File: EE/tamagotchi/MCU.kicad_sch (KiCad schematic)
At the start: 5 parts, among them J7 TAG_CONNECT, U2 STM32G031G8Ux

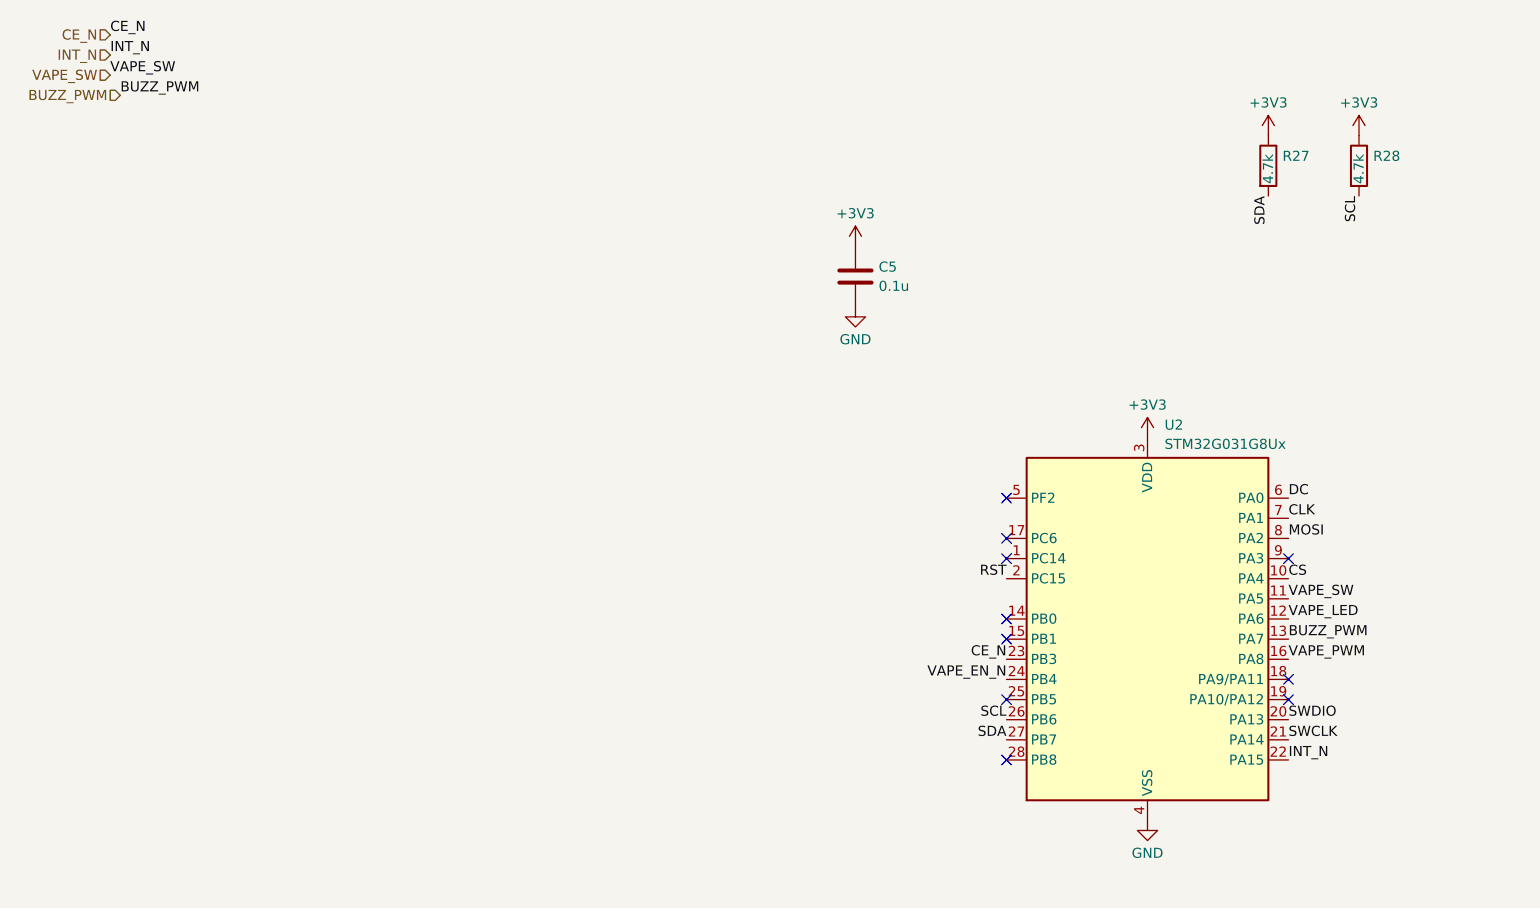
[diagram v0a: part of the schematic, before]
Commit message: WIP - Overall Cleanup, Power Change
Added expected loads for power in schematic.
Changed power arch to use existing design that appears to work.
Removed rear backlight LEDs - shouldn't be necessary.
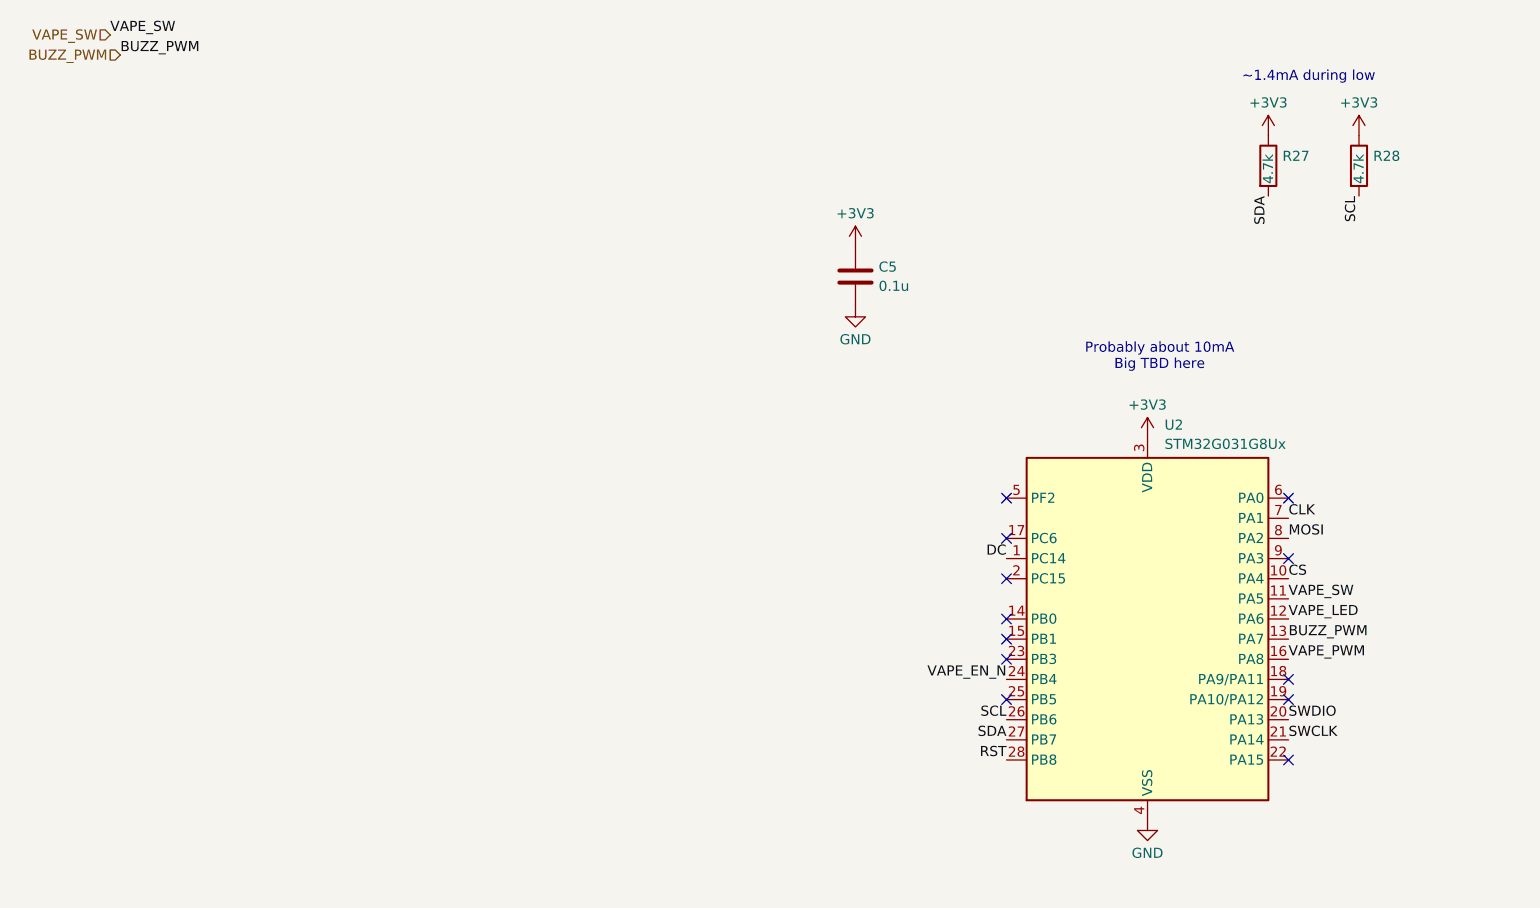
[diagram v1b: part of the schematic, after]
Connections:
- net DC: now also U2.1 (PC14); no longer U2.6 (PA0)
- net RST: now also U2.28 (PB8); no longer U2.2 (PC15)
- net CE_N: no longer names the net of U2.23 (PB3)
- net INT_N: no longer names the net of U2.22 (PA15)
- no-connect marks 12 -> 14
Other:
- note added: "Probably about 10mA Big TBD here"
- note added: "~1.4mA during low"
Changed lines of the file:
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@@
 	(generator_version "9.0")
 	(paper "A4")
+	(text "~1.4mA during low"
+		(exclude_from_sim no)
+		(at 173.99 20.574 0)
+		(effects
+			(font
+				(size 1.27 1.27)
+			)
+		)
+	)
+	(text "Probably about 10mA\nBig TBD here"
+		(exclude_from_sim no)
+		(at 155.194 55.88 0)
+		(effects
+			(font
+				(size 1.27 1.27)
+			)
+		)
+	)
 	(no_connect
 		(at 135.89 91.44)
@@
 	)
 	(no_connect
+		(at 171.45 73.66)
+	)
+	(no_connect
 		(at 135.89 73.66)
 	)
 	(no_connect
-		(at 135.89 106.68)
+		(at 135.89 83.82)
 	)
 	(no_connect
@@
 	)
 	(no_connect
-		(at 135.89 81.28)
+		(at 171.45 106.68)
 	)
 	(no_connect
@@
 	(no_connect
 		(at 171.45 81.28)
+	)
+	(no_connect
+		(at 135.89 93.98)
 	)
 	(wire
@@
 		)
 	)
-	(label "INT_N"
-		(at 22.86 17.78 0)
-		(effects
-			(font
-				(size 1.27 1.27)
-			)
-			(justify left bottom)
-		)
-	)
-	(label "RST"
-		(at 135.89 83.82 180)
-		(effects
-			(font
-				(size 1.27 1.27)
-			)
-			(justify right bottom)
-		)
-	)
 	(label "VAPE_SW"
-		(at 22.86 20.32 0)
+		(at 22.86 15.24 0)
 		(effects
 			(font
@@
 		)
 	)
-	(label "INT_N"
-		(at 171.45 106.68 0)
-		(effects
-			(font
-				(size 1.27 1.27)
-			)
-			(justify left bottom)
-		)
-	)
 	(label "VAPE_LED"
 		(at 171.45 88.9 0)
@@
 	)
 	(label "BUZZ_PWM"
-		(at 24.13 22.86 0)
-		(effects
-			(font
-				(size 1.27 1.27)
-			)
-			(justify left bottom)
+		(at 24.13 17.78 0)
+		(effects
+			(font
+				(size 1.27 1.27)
+			)
+			(justify left bottom)
+		)
+	)
+	(label "DC"
+		(at 135.89 81.28 180)
+		(effects
+			(font
+				(size 1.27 1.27)
+			)
+			(justify right bottom)
 		)
 	)
@@
 		)
 	)
+	(label "RST"
+		(at 135.89 106.68 180)
+		(effects
+			(font
+				(size 1.27 1.27)
+			)
+			(justify right bottom)
+		)
+	)
 	(label "CS"
 		(at 271.78 43.18 180)
@@
 		)
 	)
-	(label "CE_N"
-		(at 22.86 15.24 0)
-		(effects
-			(font
-				(size 1.27 1.27)
-			)
-			(justify left bottom)
-		)
-	)
-	(label "DC"
-		(at 171.45 73.66 0)
-		(effects
-			(font
-				(size 1.27 1.27)
-			)
-			(justify left bottom)
-		)
-	)
 	(label "SWDIO"
 		(at 171.45 101.6 0)
@@
 		)
 	)
-	(label "CE_N"
-		(at 135.89 93.98 180)
-		(effects
-			(font
-				(size 1.27 1.27)
-			)
-			(justify right bottom)
-		)
-	)
-	(hierarchical_label "INT_N"
-		(shape input)
-		(at 22.86 17.78 180)
+	(hierarchical_label "BUZZ_PWM"
+		(shape input)
+		(at 24.13 17.78 180)
 		(effects
 			(font
@@
 		)
 	)
-	(hierarchical_label "CE_N"
+	(hierarchical_label "MOSI"
+		(shape input)
+		(at 273.05 38.1 0)
+		(effects
+			(font
+				(size 1.27 1.27)
+			)
+			(justify left)
+		)
+	)
+	(hierarchical_label "VAPE_EN_N"
+		(shape input)
+		(at 273.05 33.02 0)
+		(effects
+			(font
+				(size 1.27 1.27)
+			)
+			(justify left)
+		)
+	)
+	(hierarchical_label "VAPE_PWM"
+		(shape input)
+		(at 273.05 35.56 0)
+		(effects
+			(font
+				(size 1.27 1.27)
+			)
+			(justify left)
+		)
+	)
+	(hierarchical_label "VAPE_LED"
+		(shape input)
+		(at 274.32 54.61 0)
+		(effects
+			(font
+				(size 1.27 1.27)
+			)
+			(justify left)
+		)
+	)
+	(hierarchical_label "DC"
+		(shape input)
+		(at 273.05 45.72 0)
+		(effects
+			(font
+				(size 1.27 1.27)
+			)
+			(justify left)
+		)
+	)
+	(hierarchical_label "CLK"
+		(shape input)
+		(at 273.05 40.64 0)
+		(effects
+			(font
+				(size 1.27 1.27)
+			)
+			(justify left)
+		)
+	)
+	(hierarchical_label "RST"
+		(shape input)
+		(at 273.05 48.26 0)
+		(effects
+			(font
+				(size 1.27 1.27)
+			)
+			(justify left)
+		)
+	)
+	(hierarchical_label "SCL"
+		(shape input)
+		(at 273.05 27.94 0)
+		(effects
+			(font
+				(size 1.27 1.27)
+			)
+			(justify left)
+		)
+	)
+	(hierarchical_label "SDA"
+		(shape input)
+		(at 273.05 30.48 0)
+		(effects
+			(font
+				(size 1.27 1.27)
+			)
+			(justify left)
+		)
+	)
+	(hierarchical_label "CS"
+		(shape input)
+		(at 273.05 43.18 0)
+		(effects
+			(font
+				(size 1.27 1.27)
+			)
+			(justify left)
+		)
+	)
+	(hierarchical_label "VAPE_SW"
 		(shape input)
 		(at 22.86 15.24 180)
 		(effects
 			(font
-				(size 1.27 1.27)
-			)
-			(justify right)
-		)
-	)
-	(hierarchical_label "BUZZ_PWM"
-		(shape input)
-		(at 24.13 22.86 180)
-		(effects
-			(font
-				(size 1.27 1.27)
-			)
-			(justify right)
-		)
-	)
-	(hierarchical_label "MOSI"
-		(shape input)
-		(at 273.05 38.1 0)
-		(effects
-			(font
-				(size 1.27 1.27)
-			)
-			(justify left)
-		)
-	)
-	(hierarchical_label "VAPE_EN_N"
-		(shape input)
-		(at 273.05 33.02 0)
-		(effects
-			(font
-				(size 1.27 1.27)
-			)
-			(justify left)
-		)
-	)
-	(hierarchical_label "VAPE_PWM"
-		(shape input)
-		(at 273.05 35.56 0)
-		(effects
-			(font
-				(size 1.27 1.27)
-			)
-			(justify left)
-		)
-	)
-	(hierarchical_label "VAPE_LED"
-		(shape input)
-		(at 274.32 54.61 0)
-		(effects
-			(font
-				(size 1.27 1.27)
-			)
-			(justify left)
-		)
-	)
-	(hierarchical_label "DC"
-		(shape input)
-		(at 273.05 45.72 0)
-		(effects
-			(font
-				(size 1.27 1.27)
-			)
-			(justify left)
-		)
-	)
-	(hierarchical_label "CLK"
-		(shape input)
-		(at 273.05 40.64 0)
-		(effects
-			(font
-				(size 1.27 1.27)
-			)
-			(justify left)
-		)
-	)
-	(hierarchical_label "RST"
-		(shape input)
-		(at 273.05 48.26 0)
-		(effects
-			(font
-				(size 1.27 1.27)
-			)
-			(justify left)
-		)
-	)
-	(hierarchical_label "SCL"
-		(shape input)
-		(at 273.05 27.94 0)
-		(effects
-			(font
-				(size 1.27 1.27)
-			)
-			(justify left)
-		)
-	)
-	(hierarchical_label "SDA"
-		(shape input)
-		(at 273.05 30.48 0)
-		(effects
-			(font
-				(size 1.27 1.27)
-			)
-			(justify left)
-		)
-	)
-	(hierarchical_label "CS"
-		(shape input)
-		(at 273.05 43.18 0)
-		(effects
-			(font
-				(size 1.27 1.27)
-			)
-			(justify left)
-		)
-	)
-	(hierarchical_label "VAPE_SW"
-		(shape input)
-		(at 22.86 20.32 180)
-		(effects
-			(font

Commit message: Pre Error check, layoutcomplete
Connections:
- net VAPE_LED: now also U2.11 (PA5); no longer U2.12 (PA6)
- net VAPE_SW: now also U2.12 (PA6); no longer U2.11 (PA5)
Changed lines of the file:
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@@
-		)
-	)
-	(label "VAPE_LED"
-		(at 171.45 88.9 0)
-		(effects
-			(font
-				(size 1.27 1.27)
-			)
-			(justify left bottom)
 		)
 	)
@@
 		)
 	)
+	(label "VAPE_SW"
+		(at 171.45 88.9 0)
+		(effects
+			(font
+				(size 1.27 1.27)
+			)
+			(justify left bottom)
+		)
+	)
 	(label "DC"
 		(at 135.89 81.28 180)
@@
 			)
 			(justify right bottom)
-		)
-	)
-	(label "VAPE_SW"
-		(at 171.45 86.36 0)
-		(effects
-			(font
-				(size 1.27 1.27)
-			)
-			(justify left bottom)
 		)
 	)
@@
 		)
 	)
+	(label "VAPE_LED"
+		(at 171.45 86.36 0)
+		(effects
+			(font
+				(size 1.27 1.27)
+			)
+			(justify left bottom)
+		)
+	)
